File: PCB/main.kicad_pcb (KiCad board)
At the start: 4 copper layers, 86.6 x 50.5 mm, 63 parts, among them J1 S20B-PADSS-1, J2 S20B-PADSS-1, J3 SWD, SW1 SPST, U1 TPS5430, U2 AMS1117-3.3, U3 MCP2558FD, U4 MCP2558FD, U5 STM32G0B1, Y1 40M

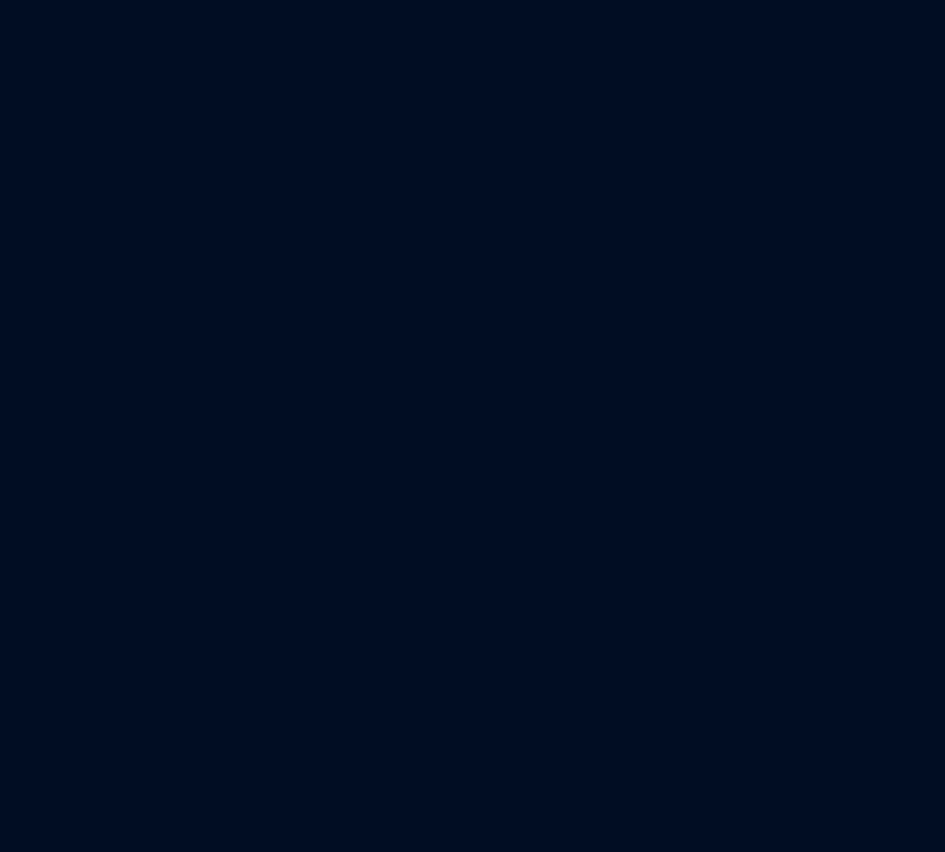
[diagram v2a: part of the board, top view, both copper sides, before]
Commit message: Start moving to TPS54302
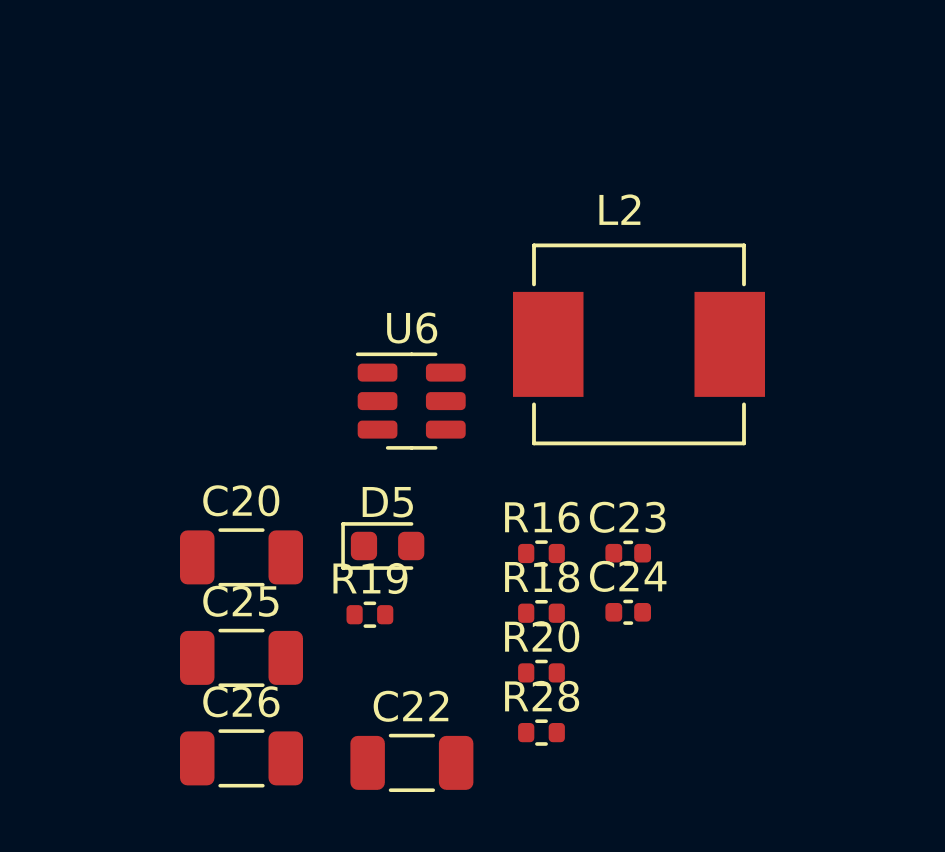
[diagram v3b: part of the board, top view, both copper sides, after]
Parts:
- added C20: 22u, Capacitor_SMD:C_1206_3216Metric, F.Cu at (43.8, 115.1)
- added C22: 22u, Capacitor_SMD:C_1206_3216Metric, F.Cu at (49.5, 122.0)
- added C23: 100n, Capacitor_SMD:C_0402_1005Metric, F.Cu at (56.7, 115.0)
- added C24: 47p, Capacitor_SMD:C_0402_1005Metric, F.Cu at (56.7, 116.9)
- added C25: 22u, Capacitor_SMD:C_1206_3216Metric, F.Cu at (43.8, 118.5)
- added C26: 22u, Capacitor_SMD:C_1206_3216Metric, F.Cu at (43.8, 121.8)
- added D5: LED_B, LED_SMD:LED_0603_1608Metric, F.Cu at (48.7, 114.7)
- added L2: 8.2u, libdb:CMP-0058, F.Cu at (57.1, 108.0)
- added R16: 510k, Resistor_SMD:R_0402_1005Metric, F.Cu at (53.8, 115.0)
- added R18: 100k, Resistor_SMD:R_0402_1005Metric, F.Cu at (53.8, 117.0)
- added R19: 470, Resistor_SMD:R_0402_1005Metric, F.Cu at (48.1, 117.0)
- added R20: 5.1k, Resistor_SMD:R_0402_1005Metric, F.Cu at (53.8, 119.0)
- added R28: 39k, Resistor_SMD:R_0402_1005Metric, F.Cu at (53.8, 120.9)
- added U6: TPS54302, Package_TO_SOT_SMD:SOT-23-6, F.Cu at (49.5, 109.9)
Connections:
- C5 pad 1: +5V -> Net-(C5-Pad1)
- C6 pad 1: +5V -> Net-(C5-Pad1)
- L1 pad 2: +5V -> Net-(C5-Pad1)
- R1 pad 1: +5V -> Net-(C5-Pad1)
- R3 pad 1: +5V -> Net-(C5-Pad1)
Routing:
- net Net-(C5-Pad1): track 0.00 -> 14.4 mm, vias 0 -> 2
- net +5V: track 20.7 -> 6.33 mm, vias 2 -> 0

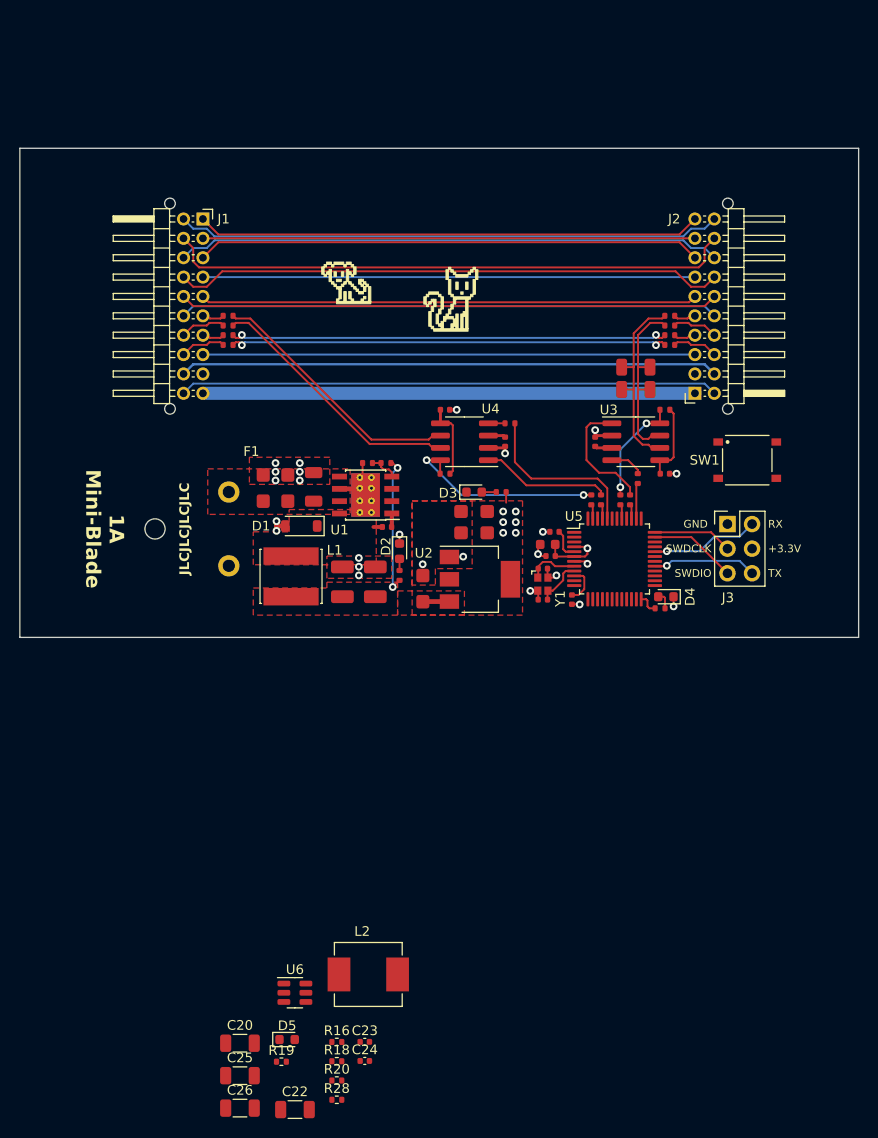
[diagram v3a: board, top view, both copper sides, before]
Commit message: Re-layout with TPS54302
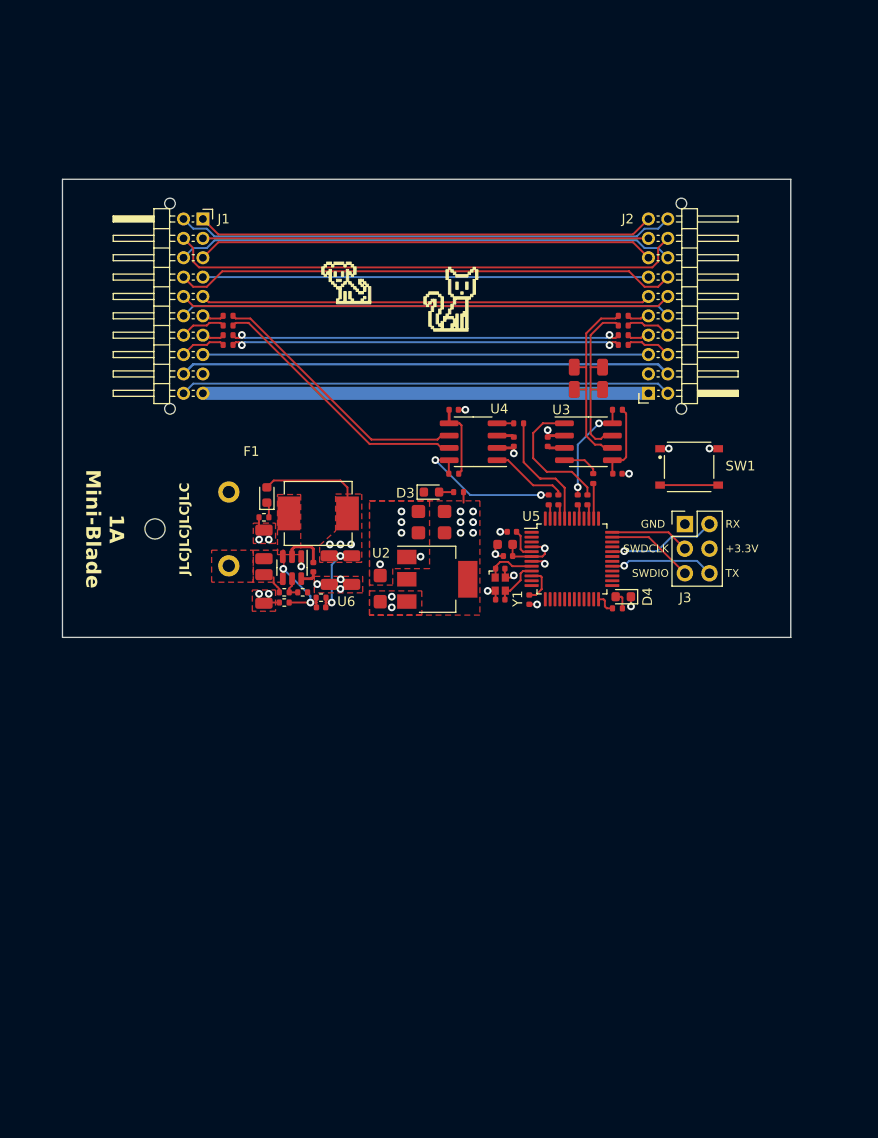
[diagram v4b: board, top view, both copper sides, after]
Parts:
- removed C1, C2: 10u, Capacitor_Tantalum_SMD:CP_EIA-3216-18_Kemet-A
- removed C3: 22u, Capacitor_SMD:C_1206_3216Metric
- removed C4: 10n, Capacitor_SMD:C_0402_1005Metric
- removed C5, C6: 100u, Capacitor_Tantalum_SMD:CP_EIA-3528-15_AVX-H
- removed D1: B5819W, Diode_SMD:D_SOD-123
- removed D2: LED_B, LED_SMD:LED_0603_1608Metric
- removed L1: 33u, libdb:CMP-0036
- removed R1: 6.8k, Resistor_SMD:R_0402_1005Metric
- removed R2: 2.2k, Resistor_SMD:R_0402_1005Metric
- removed R3: 470, Resistor_SMD:R_0402_1005Metric
- removed U1: TPS5430, libdb:CMP-0030
- moved C22 58.4 mm to (46.3, 63.6), turned to 90 degrees
- moved C26 56.3 mm to (53.0, 66.2), turned to -90 degrees
- moved D5 56.3 mm to (46.6, 58.5), turned to 90 degrees
- moved R19 56.2 mm to (46.3, 60.8), turned to 180 degrees
- moved C25 53.5 mm to (55.4, 66.2), turned to -90 degrees
- moved R28 51.9 mm to (52.2, 69.1), turned to 180 degrees
- moved R20 49.6 mm to (48.4, 69.6), turned to 180 degrees
- moved C23 49.3 mm to (51.4, 66.0), turned to 90 degrees
- moved R18 48.5 mm to (50.3, 68.5)
- moved L2 47.9 mm to (51.9, 60.4)
- moved C24 47.0 mm to (52.2, 70.1), turned to 180 degrees
- moved C20 47.0 mm to (46.3, 68.2), turned to -90 degrees
- moved R16 46.7 mm to (48.4, 68.5)
- moved U6 43.9 mm to (49.2, 66.0), turned to -90 degrees
- moved REF** 6.80 mm to (102.7, 73.1)
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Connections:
- D5 pad 1: GND -> Net-(D5-K)
- D5 pad 2: Net-(D5-A) -> +5V
- F1 pad 1: +BATT -> /JST_10_BAT+
- F1 pad 2: /JST_10_BAT+ -> +BATT
- R19 pad 1: +5V -> Net-(D5-K)
- R19 pad 2: Net-(D5-A) -> GND
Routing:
- net +5V: track 6.33 -> 22.0 mm, vias 0 -> 7
- net Net-(C5-Pad1): track 14.4 -> 0.00 mm, vias 2 -> 0
- net Net-(U6-FB): track 0.00 -> 9.49 mm, vias 0 -> 2
- net Net-(U5-PF2): track 3.86 -> 9.86 mm
- net /FDCAN2_S: track 21.3 -> 16.0 mm
- net /FDCAN2_TX: track 13.3 -> 8.04 mm
- net /FDCAN2_RX: track 17.8 -> 12.5 mm
- net /JST_13_AUDIO_FL: track 56.3 -> 51.5 mm
- net /FW_CAN2+: track 45.3 -> 40.5 mm
- net /JST_14_AUDIO_FL: track 57.0 -> 52.2 mm
- net /JST_19_CAM_12V+: track 55.6 -> 50.8 mm
- net /JST_16_NC: track 55.6 -> 50.8 mm
- net /JST_15_VID_IN: track 55.6 -> 50.8 mm
- net /JST_12_AUDIO_FL: track 58.9 -> 54.1 mm
- net /JST_11_AUDIO_FL: track 56.3 -> 51.5 mm
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- added copper zone on In2.Cu, net +5V
- added copper zone on F.Cu, net Net-(U6-SW)
- removed copper zone on F.Cu, net /PH
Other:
- board size 86.6 x 50.5 mm -> 75.2 x 47.3 mm

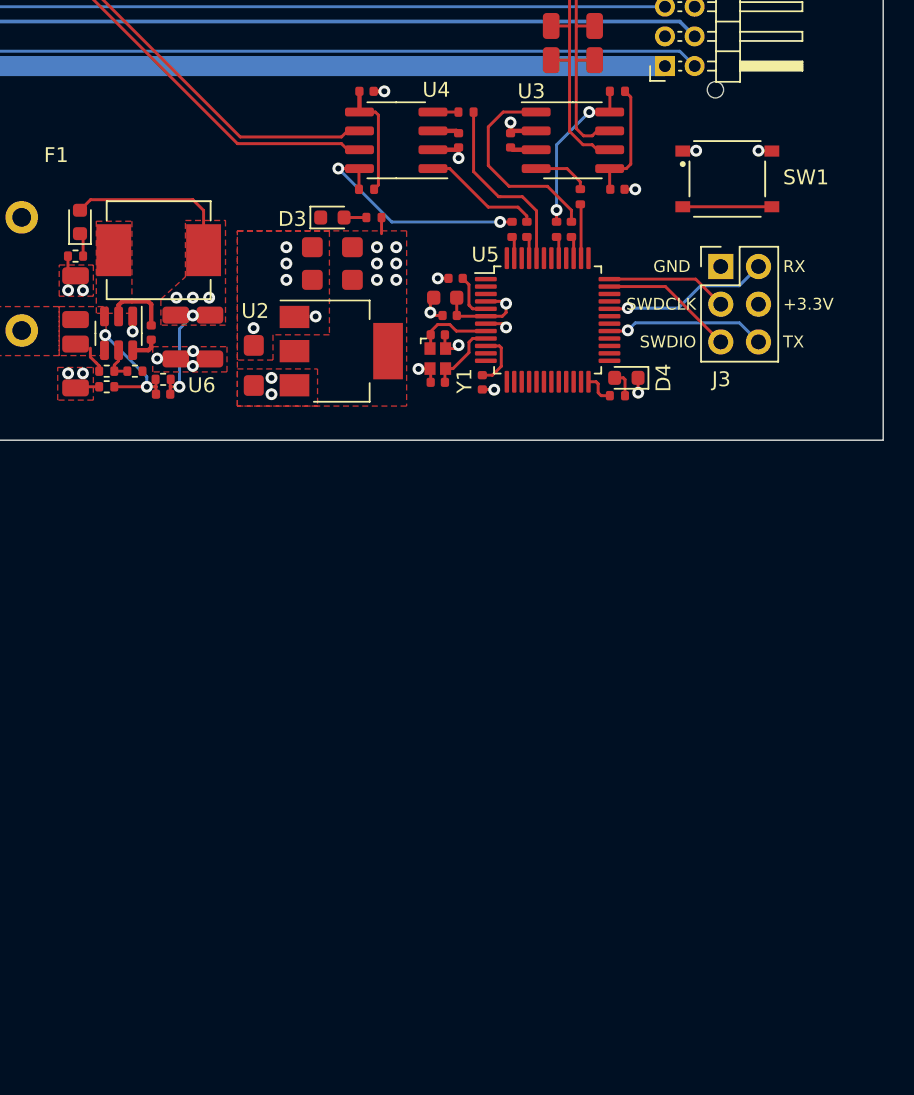
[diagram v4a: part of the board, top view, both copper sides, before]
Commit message: Start changing LDO
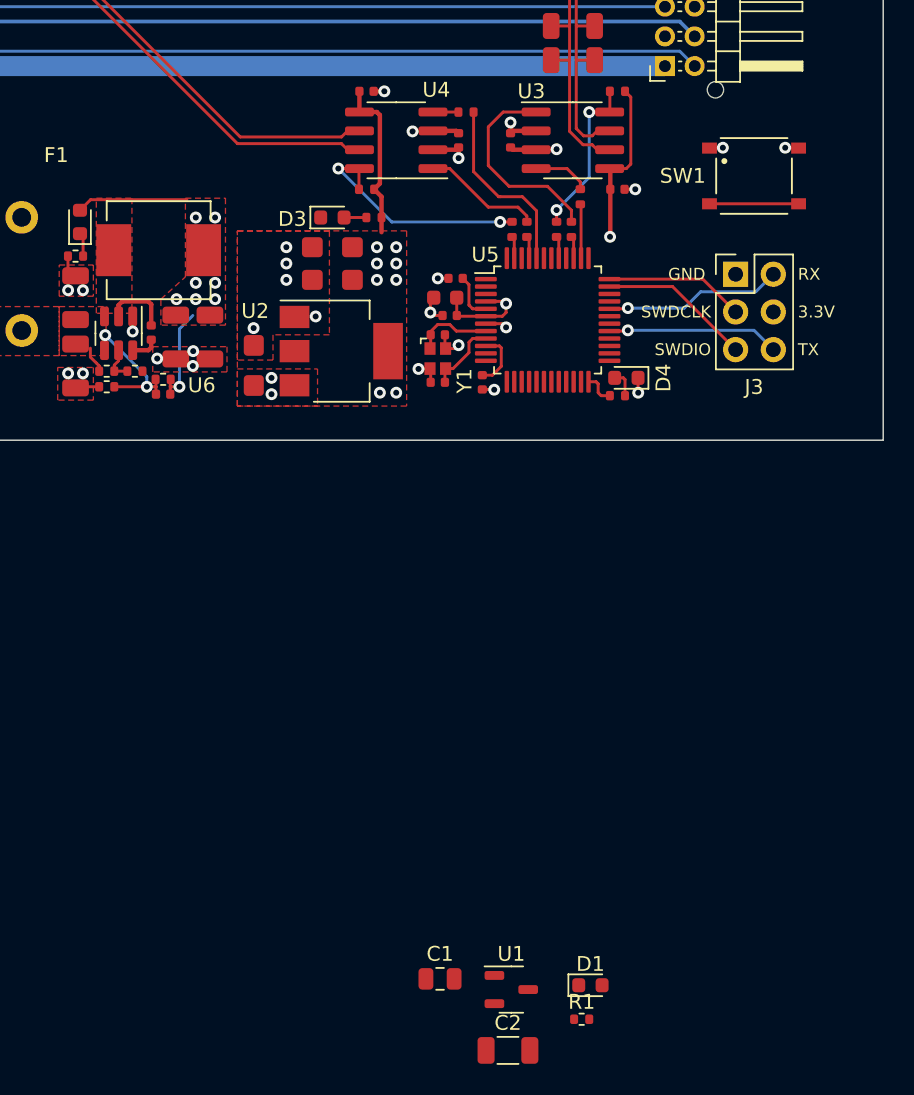
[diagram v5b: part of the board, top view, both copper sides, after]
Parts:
- added C1: 1u, Capacitor_SMD:C_0805_2012Metric, F.Cu at (70.8, 109.5)
- added C2: 22u, Capacitor_SMD:C_1206_3216Metric, F.Cu at (75.4, 114.3)
- added D1: LED_B, LED_SMD:LED_0603_1608Metric, F.Cu at (81.0, 109.9)
- added R1: 100, Resistor_SMD:R_0402_1005Metric, F.Cu at (80.4, 112.2)
- added U1: XC6206P33, libdb:CMP-0019, F.Cu at (75.7, 110.2)
- moved SW1 1.81 mm to (92.0, 55.4)
- moved J3 1.13 mm to (90.8, 62.0)
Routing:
- net +3.3V: track 23.5 -> 29.0 mm, vias 7 -> 10
- net +5V: track 22.0 -> 20.7 mm, vias 7 -> 12
- net /SWDIO: track 9.04 -> 10.3 mm
- net /SWDCLK: track 8.20 -> 9.41 mm
- net /USART1_TX: track 10.8 -> 11.6 mm
- net /USART1_RX: track 11.2 -> 12.0 mm

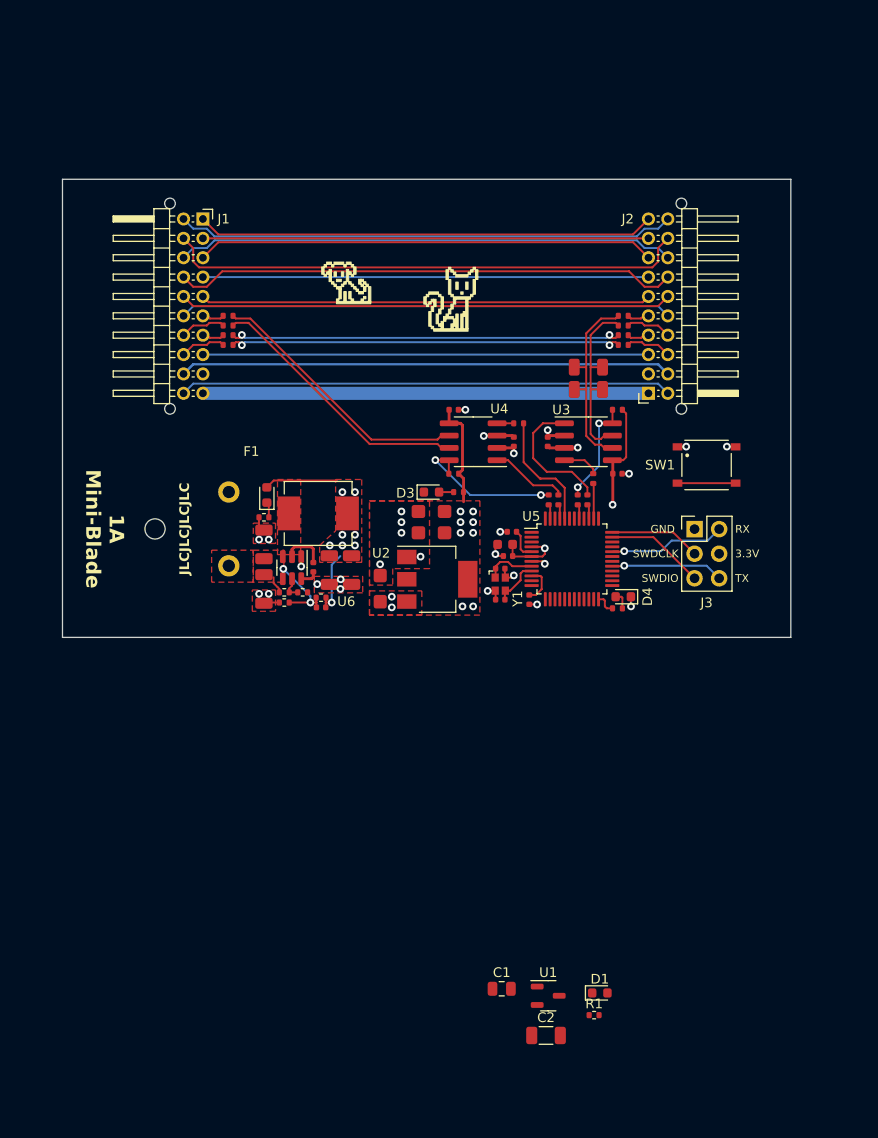
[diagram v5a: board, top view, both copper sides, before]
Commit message: Further development, started final GND pour
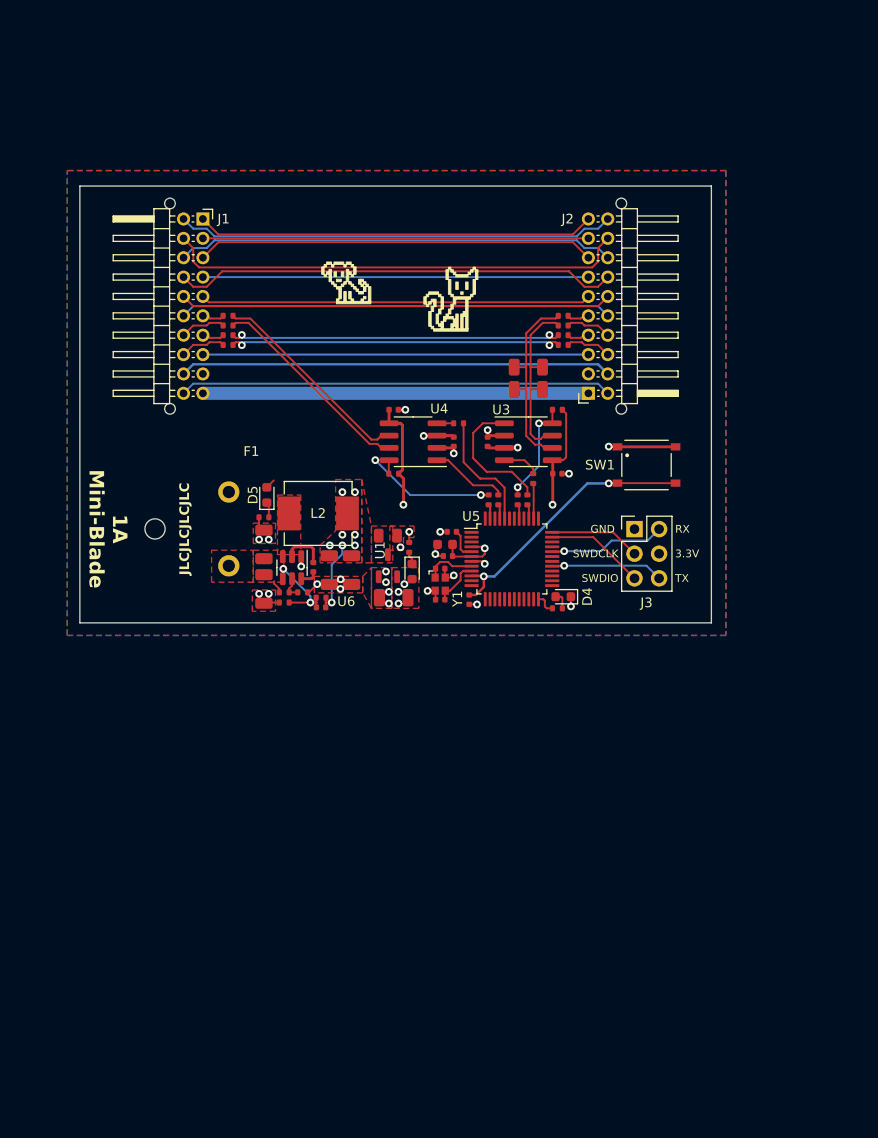
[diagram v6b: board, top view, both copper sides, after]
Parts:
- removed C7, C8, C9: 10u, Capacitor_Tantalum_SMD:CP_EIA-3216-18_Kemet-A
- removed D3: LED_B, LED_SMD:LED_0603_1608Metric
- removed R4: 100, Resistor_SMD:R_0402_1005Metric
- removed U2: AMS1117-3.3, Package_TO_SOT_SMD:SOT-223-3_TabPin2
- moved R1 51.9 mm to (61.3, 63.9), turned to -90 degrees
- moved C1 48.2 mm to (59.1, 62.7)
- moved C2 47.9 mm to (59.7, 69.1), turned to 180 degrees
- moved D1 47.6 mm to (61.6, 66.4), turned to -90 degrees
- moved U1 47.4 mm to (59.1, 65.8), turned to 90 degrees
- moved C10 6.20 mm to (76.6, 56.3)
- moved C12 6.20 mm to (59.7, 49.7)
- moved C14 6.20 mm to (65.0, 63.6)
- moved C15 6.20 mm to (65.3, 64.8)
- moved C16 6.20 mm to (65.7, 62.3)
- moved C17 6.20 mm to (64.5, 69.3)
- moved C18 6.20 mm to (64.5, 66.1)
- moved C19 6.20 mm to (67.5, 69.3)
- moved D4 6.20 mm to (77.2, 69.0)
- moved J2 6.20 mm to (79.8, 48.0)
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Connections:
- C1 pad 1: Net-(U1-VI) -> +5V
- D1 pad 1: GND -> Net-(D1-K)
- D1 pad 2: Net-(D1-A) -> +3.3V
- R1 pad 1: Net-(D1-A) -> GND
- R1 pad 2: +3.3V -> Net-(D1-K)
- U1 pad 3: Net-(U1-VI) -> +5V
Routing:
- net Net-(U5-PF2): track 9.86 -> 28.0 mm, vias 0 -> 2
- net GND: track 22.2 -> 29.7 mm
- net /JST_20_NC: track 50.8 -> 44.6 mm
- net /JST_13_AUDIO_FL: track 51.5 -> 45.3 mm
- net /JST_19_CAM_12V+: track 50.8 -> 44.6 mm
- net /JST_16_NC: track 50.8 -> 44.6 mm
- net /JST_15_VID_IN: track 50.8 -> 44.6 mm
- net /JST_14_AUDIO_FL: track 52.2 -> 46.0 mm
- net /JST_12_AUDIO_FL: track 54.1 -> 47.9 mm
- net /JST_11_AUDIO_FL: track 51.5 -> 45.3 mm
- net /JST_10_BAT+: track 46.0 -> 39.8 mm
- net /JST_08_CAM_DET: track 46.0 -> 39.8 mm
- net /JST_04_NC: track 46.0 -> 39.8 mm
- net /JST_03_AUX_IN: track 47.3 -> 41.1 mm
- net /JST_02_AUX_IN: track 46.0 -> 39.8 mm
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- added copper zone on B.Cu, net GND
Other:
- board size 75.2 x 47.3 mm -> 65.2 x 45.1 mm
